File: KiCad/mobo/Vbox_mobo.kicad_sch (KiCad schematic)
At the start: 46 parts, among them J1 Conn_01x02, J10 Conn_01x01, J11 Conn_01x01, J12 Conn_01x02, J13 Conn_01x02, J14 Conn_01x02, J15 Conn_01x02, J2 DuPont Connector, J2 JTAG_TC2030, J4 Conn_01x06, J5 Conn_01x06, J6 Conn_01x10, J7 Conn_01x10, J8 Conn_01x01, J9 Conn_01x01, SW1 Boot, U1 XC6206, U2 X05A26H12G, U3 RP2040, U4 W25Q128JVS, Y1 12MHz

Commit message: fix up unpopulated components on bom
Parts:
- J10, J11, J12, J13, J14, J15, J8, J9: now left out of the parts list
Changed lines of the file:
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@@
   )
   (symbol (lib_id "Connector_Generic:Conn_01x02") (at 190.5 115.57 0) (mirror x) (unit 1)
-    (in_bom yes) (on_board yes) (dnp no)
+    (in_bom no) (on_board yes) (dnp no)
     (property "Reference" "J14" (at 193.04 113.03 0)
       (effects (font (size 1.27 1.27)) (justify left))
@@
   )
   (symbol (lib_id "Connector_Generic:Conn_01x01") (at 190.5 134.62 0) (unit 1)
-    (in_bom yes) (on_board yes) (dnp no) (fields_autoplaced)
+    (in_bom no) (on_board yes) (dnp no) (fields_autoplaced)
     (property "Reference" "J10" (at 193.04 133.35 0)
       (effects (font (size 1.27 1.27)) (justify left))
@@
   )
   (symbol (lib_id "Connector_Generic:Conn_01x02") (at 190.5 100.33 0) (mirror x) (unit 1)
-    (in_bom yes) (on_board yes) (dnp no)
+    (in_bom no) (on_board yes) (dnp no)
     (property "Reference" "J12" (at 193.04 97.79 0)
       (effects (font (size 1.27 1.27)) (justify left))
@@
   )
   (symbol (lib_id "Connector_Generic:Conn_01x02") (at 213.36 100.33 0) (mirror x) (unit 1)
-    (in_bom yes) (on_board yes) (dnp no)
+    (in_bom no) (on_board yes) (dnp no)
     (property "Reference" "J13" (at 215.9 97.79 0)
       (effects (font (size 1.27 1.27)) (justify left))
@@
   )
   (symbol (lib_id "Connector_Generic:Conn_01x01") (at 190.5 125.73 0) (unit 1)
-    (in_bom yes) (on_board yes) (dnp no) (fields_autoplaced)
+    (in_bom no) (on_board yes) (dnp no) (fields_autoplaced)
     (property "Reference" "J8" (at 193.04 124.46 0)
       (effects (font (size 1.27 1.27)) (justify left))
@@
   )
   (symbol (lib_id "Connector_Generic:Conn_01x02") (at 213.36 115.57 0) (mirror x) (unit 1)
-    (in_bom yes) (on_board yes) (dnp no)
+    (in_bom no) (on_board yes) (dnp no)
     (property "Reference" "J15" (at 215.9 113.03 0)
       (effects (font (size 1.27 1.27)) (justify left))
@@
   )
   (symbol (lib_id "Connector_Generic:Conn_01x01") (at 218.44 134.62 0) (unit 1)
-    (in_bom yes) (on_board yes) (dnp no) (fields_autoplaced)
+    (in_bom no) (on_board yes) (dnp no) (fields_autoplaced)
     (property "Reference" "J11" (at 220.98 133.35 0)
       (effects (font (size 1.27 1.27)) (justify left))
@@
   )
   (symbol (lib_id "Connector_Generic:Conn_01x01") (at 218.44 125.73 0) (unit 1)
-    (in_bom yes) (on_board yes) (dnp no) (fields_autoplaced)
+    (in_bom no) (on_board yes) (dnp no) (fields_autoplaced)
     (property "Reference" "J9" (at 220.98 124.46 0)
       (effects (font (size 1.27 1.27)) (justify left))

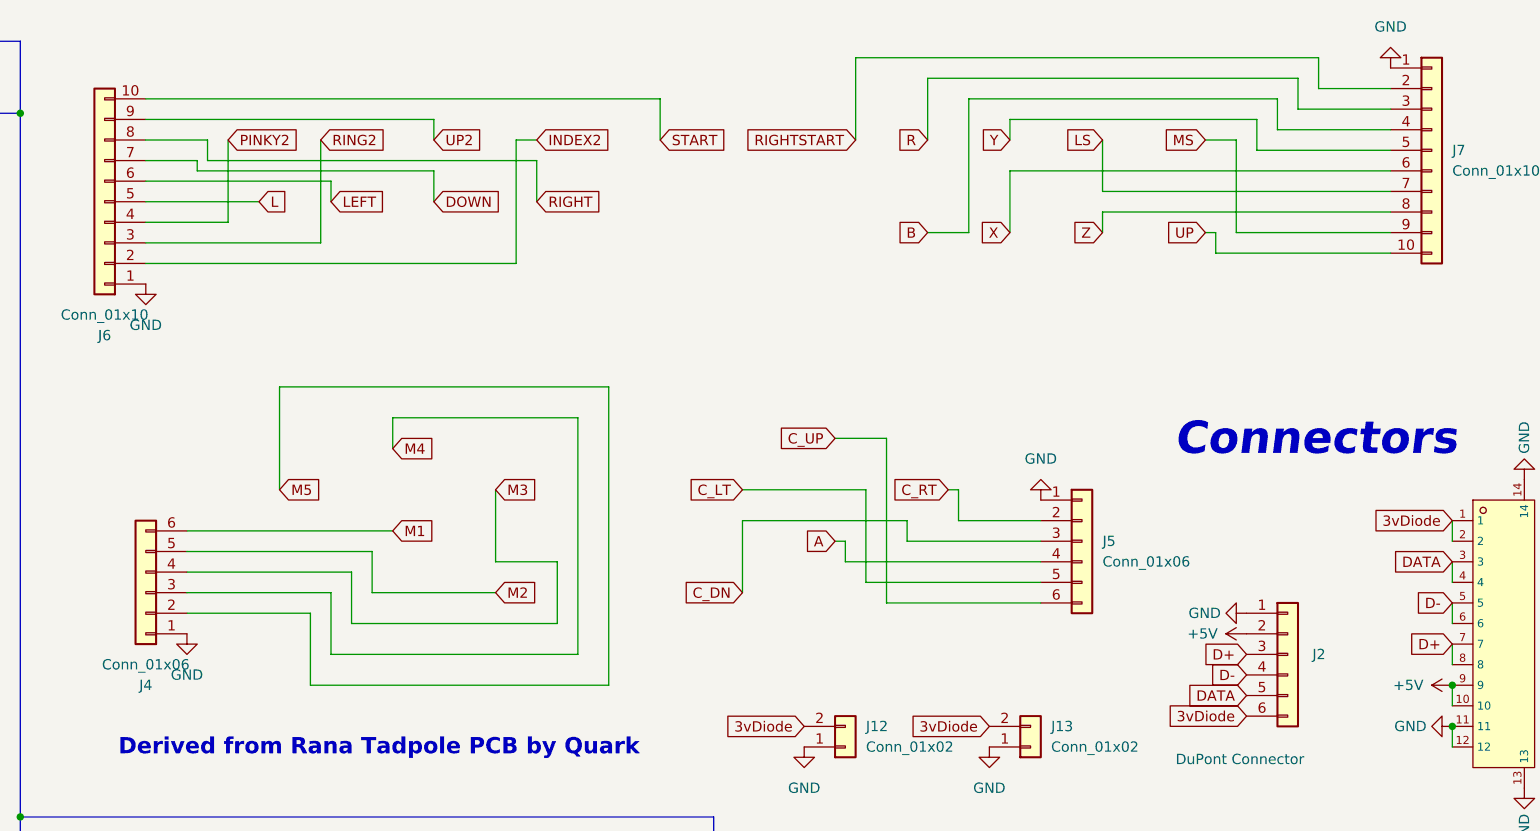
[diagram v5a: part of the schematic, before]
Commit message: adjust finger ergo, pullup resistors on mobo
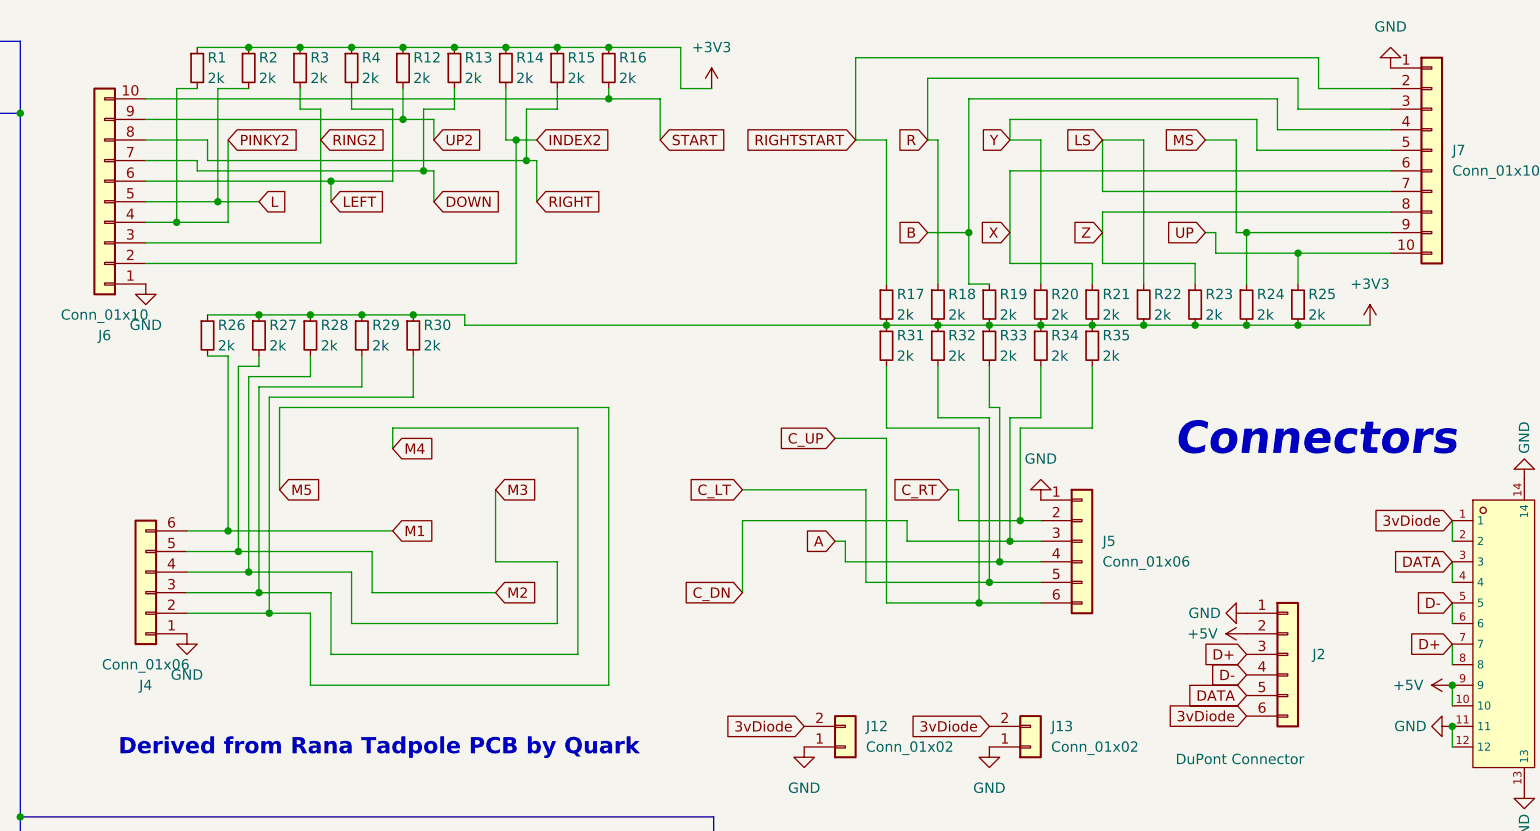
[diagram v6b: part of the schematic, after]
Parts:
- added R1, R12, R13, R14, R15, R16, R17, R18, R19, R2, R20, R21, R22, R23, R24, R25, R26, R27, R28, R29, R3, R30, R31, R32, R33, R34, R35, R4: 2k, Resistor_SMD:R_0402_1005Metric, symbol Device:R_Small
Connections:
- net +3V3: now also R1.1, R12.1, R13.1, R14.1, R15.1, R16.1, R17.2, R18.2, R19.2, R2.1, R20.2, R21.2, R22.2, R23.2, R24.2, R25.2, R26.1, R27.1, R28.1, R29.1, R3.1, R30.1, R31.1, R32.1, R33.1, R34.1, R35.1, R4.1
- net A: now also R33.2
- net B: now also R19.1
- net C_DN: now also R34.2
- net C_LT: now also R32.2
- net C_RT: now also R35.2
- net C_UP: now also R31.2
- net DOWN: now also R13.2
- net INDEX2: now also R14.2
- net L: now also R2.2
- net LEFT: now also R4.2
- net LS: now also R22.1
- net M1: now also R26.2
- net M2: now also R27.2
- net M3: now also R28.2
- net M4: now also R29.2
- net M5: now also R30.2
- net MS: now also R24.1
- net PINKY2: now also R1.2
- net R: now also R18.1
- net RIGHT: now also R15.2
- net RIGHTSTART: now also R17.1
- net RING2: now also R3.2
- net START: now also R16.2
- net UP: now also R25.1
- net UP2: now also R12.2
- net X: now also R21.1
- net Y: now also R20.1
- net Z: now also R23.1

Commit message: not sure what this change was
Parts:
- J1, J12, J13, J14, J15: now not fitted
- R1, R12, R13, R14, R15, R16, R17, R18, R19, R2, R20, R21, R22, R23, R24, R25, R26, R27, R28, R29, R3, R30, R31, R32, R33, R34, R35, R4: LCSC (none) -> C25552
